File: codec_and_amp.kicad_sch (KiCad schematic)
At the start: 31 parts, among them J1 Conn_01x08, J2 Conn_01x06, U1 TLV320AIC3206IRSBR, U4 FSA2275UMX, U6 TLV7111830DSER, U7 TPD4E02B04DQAR, U8 TPD4E02B04DQAR

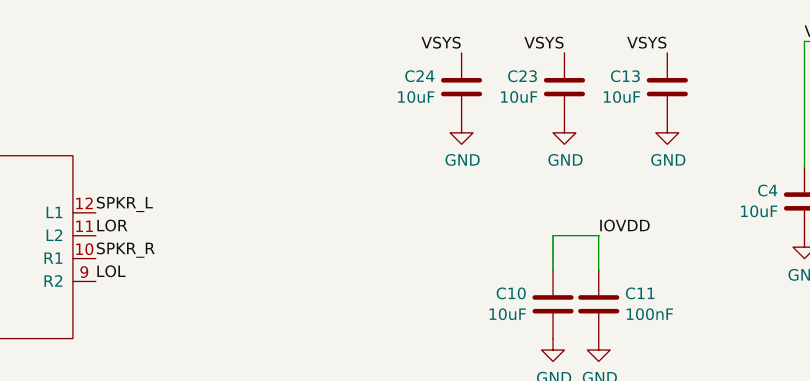
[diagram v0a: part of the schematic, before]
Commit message: Change DSI connector to the 15-pin standard instead of 22-pin standard
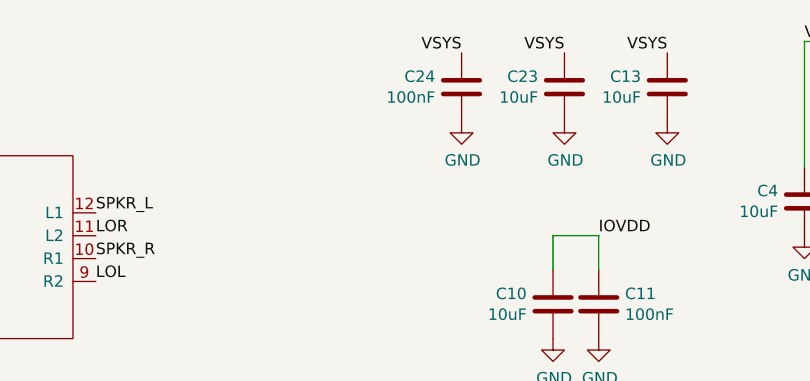
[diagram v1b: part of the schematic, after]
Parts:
- C24: value 10uF -> 100nF
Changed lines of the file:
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@@
       (effects (font (size 1.27 1.27)) (justify right))
     )
-    (property "Value" "10uF" (id 1) (at 191.389 22.733 0)
+    (property "Value" "100nF" (id 1) (at 191.389 22.733 0)
       (effects (font (size 1.27 1.27)) (justify right))
     )

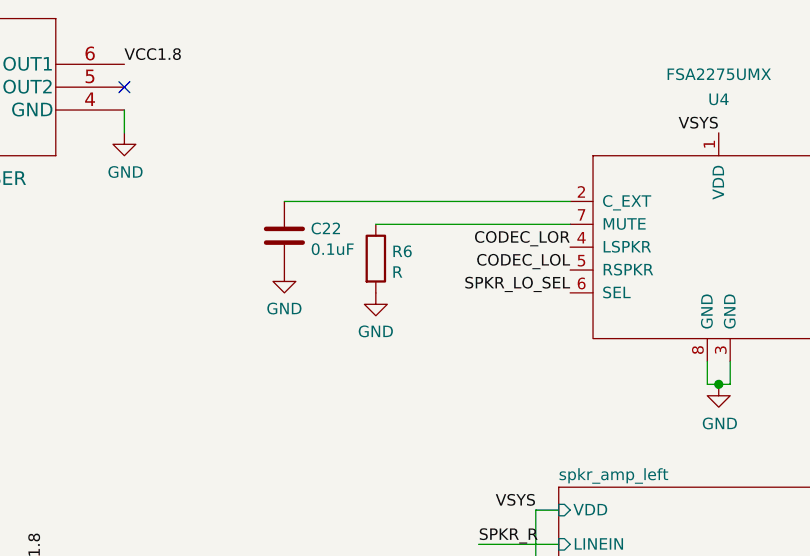
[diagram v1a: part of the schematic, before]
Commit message: Switch some footprints to minimize BOM costs. Cache a bunch more datasheets and documentation
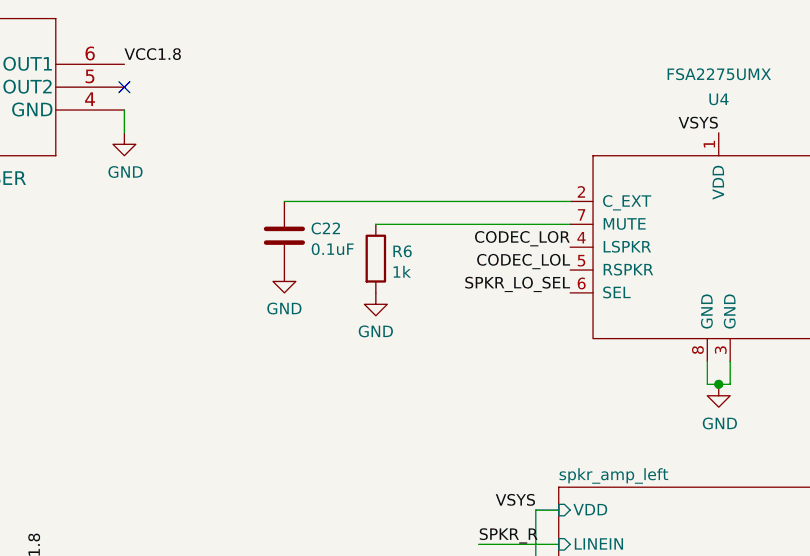
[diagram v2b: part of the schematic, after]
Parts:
- R6: value R -> 1k
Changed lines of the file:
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@@
       (effects (font (size 1.27 1.27)) (justify left))
     )
-    (property "Value" "R" (id 1) (at 100.8381 42.1778 0)
+    (property "Value" "1k" (id 1) (at 100.8381 42.1778 0)
       (effects (font (size 1.27 1.27)) (justify left))
     )

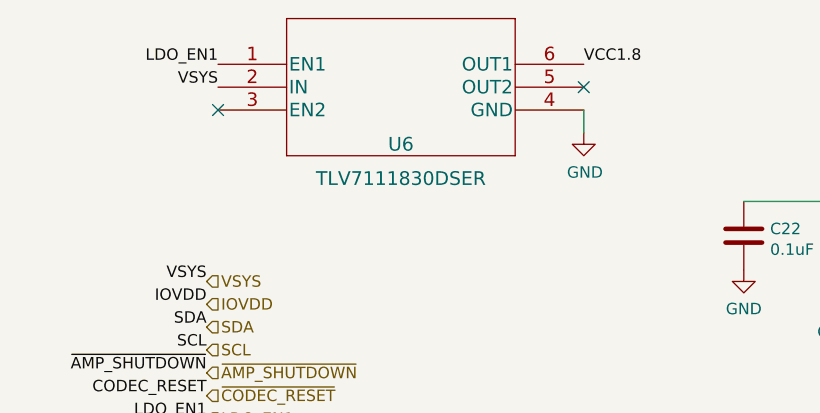
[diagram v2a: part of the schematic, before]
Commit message: Replace TLV7111830 with MIC5504, since I wasn't using that VCC3.0 and the tlv7111830 is out of stock.
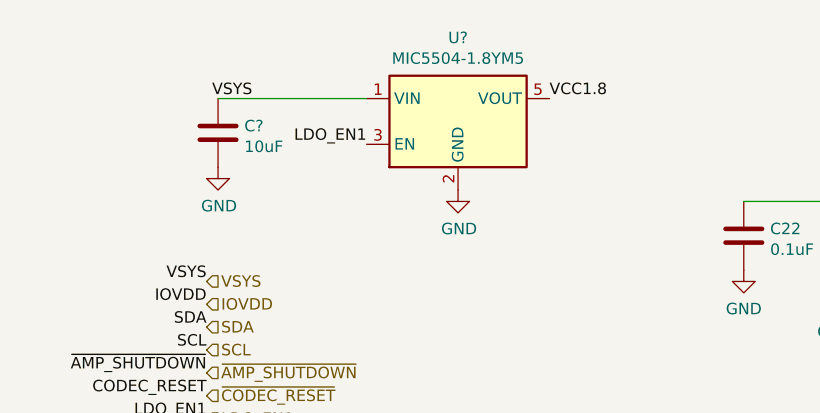
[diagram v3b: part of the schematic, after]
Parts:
- removed U6: TLV7111830DSER, footprints:TLV7111830DSER, symbol TLV7111830DSER:TLV7111830DSER
- added C?: 10uF, Capacitor_SMD:C_0402_1005Metric, symbol Device:C
- added U?: MIC5504-1.8YM5, Package_TO_SOT_SMD:SOT-23-5, symbol Regulator_Linear:MIC5504-1.8YM5
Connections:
- net GND: now also C?.2, U?.2 (GND)
- net LDO_EN1: now also U?.3 (EN)
- net VCC1.8: now also U?.5 (VOUT)
- net VSYS: now also C?.1, U?.1 (VIN)
- no-connect marks 7 -> 5
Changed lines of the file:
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@@
   (no_connect (at 29.21 104.14))
   (no_connect (at 29.21 124.46))
-  (no_connect (at 30.48 24.13))
-  (no_connect (at 71.12 21.59))
   (no_connect (at 85.09 116.84))
   (no_connect (at 85.09 139.7))
@@
     (stroke (width 0) (type solid) (color 0 0 0 0))
   )
+  (wire (pts (xy 30.48 22.86) (xy 46.99 22.86))
+    (stroke (width 0) (type solid) (color 0 0 0 0))
+  )
   (wire (pts (xy 52.07 167.64) (xy 54.61 167.64))
     (stroke (width 0) (type solid) (color 0 0 0 0))
@@
     (stroke (width 0) (type solid) (color 0 0 0 0))
   )
-  (wire (pts (xy 71.12 24.13) (xy 71.12 26.67))
-    (stroke (width 0) (type solid) (color 0 0 0 0))
-  )
   (wire (pts (xy 85.09 120.65) (xy 95.25 120.65))
     (stroke (width 0) (type solid) (color 0 0 0 0))
@@
     (effects (font (size 1.27 1.27)) (justify right bottom))
   )
-  (label "LDO_EN1" (at 30.48 19.05 180)
-    (effects (font (size 1.27 1.27)) (justify right bottom))
-  )
-  (label "VSYS" (at 30.48 21.59 180)
+  (label "VSYS" (at 34.29 22.86 180)
+    (effects (font (size 1.27 1.27)) (justify right bottom))
+  )
+  (label "LDO_EN1" (at 46.99 27.94 180)
     (effects (font (size 1.27 1.27)) (justify right bottom))
   )
@@
     (effects (font (size 1.27 1.27)) (justify left bottom))
   )
-  (label "VCC1.8" (at 71.12 19.05 0)
+  (label "VCC1.8" (at 67.31 22.86 0)
     (effects (font (size 1.27 1.27)) (justify left bottom))
   )
@@
     (pin "1")
   )
+  (symbol (lib_id "power:GND") (at 30.48 30.48 0) (unit 1)
+    (in_bom yes) (on_board yes)
+    (property "Reference" "#PWR?" (id 0) (at 30.48 36.83 0)
+      (effects (font (size 1.27 1.27)) hide)
+    )
+    (property "Value" "GND" (id 1) (at 30.5943 34.8044 0))
+    (property "Footprint" "" (id 2) (at 30.48 30.48 0)
+      (effects (font (size 1.27 1.27)) hide)
+    )
+    (property "Datasheet" "" (id 3) (at 30.48 30.48 0)
+      (effects (font (size 1.27 1.27)) hide)
+    )
+    (pin "1")
+  )
   (symbol (lib_id "power:GND") (at 38.1 175.26 0) (unit 1)
     (in_bom yes) (on_board yes)
@@
     (pin "1")
   )
+  (symbol (lib_id "power:GND") (at 57.15 33.02 0) (unit 1)
+    (in_bom yes) (on_board yes)
+    (property "Reference" "#PWR?" (id 0) (at 57.15 39.37 0)
+      (effects (font (size 1.27 1.27)) hide)
+    )
+    (property "Value" "GND" (id 1) (at 57.2643 37.3444 0))
+    (property "Footprint" "" (id 2) (at 57.15 33.02 0)
+      (effects (font (size 1.27 1.27)) hide)
+    )
+    (property "Datasheet" "" (id 3) (at 57.15 33.02 0)
+      (effects (font (size 1.27 1.27)) hide)
+    )
+    (pin "1")
+  )
   (symbol (lib_id "power:GND") (at 58.42 167.64 0) (unit 1)
     (in_bom yes) (on_board yes)
@@
     )
     (property "Datasheet" "" (id 3) (at 58.42 167.64 0)
-      (effects (font (size 1.27 1.27)) hide)
-    )
-    (pin "1")
-  )
-  (symbol (lib_id "power:GND") (at 71.12 26.67 0) (unit 1)
-    (in_bom yes) (on_board yes)
-    (property "Reference" "#PWR0111" (id 0) (at 71.12 33.02 0)
-      (effects (font (size 1.27 1.27)) hide)
-    )
-    (property "Value" "GND" (id 1) (at 71.247 31.0642 0))
-    (property "Footprint" "" (id 2) (at 71.12 26.67 0)
-      (effects (font (size 1.27 1.27)) hide)
-    )
-    (property "Datasheet" "" (id 3) (at 71.12 26.67 0)
       (effects (font (size 1.27 1.27)) hide)
     )
@@
     )
     (property "Datasheet" "~" (id 3) (at 99.06 40.64 0)
+      (effects (font (size 1.27 1.27)) hide)
+    )
+    (pin "1")
+    (pin "2")
+  )
+  (symbol (lib_id "Device:C") (at 30.48 26.67 0) (unit 1)
+    (in_bom yes) (on_board yes) (fields_autoplaced)
+    (property "Reference" "C?" (id 0) (at 33.4011 25.9091 0)
+      (effects (font (size 1.27 1.27)) (justify left))
+    )
+    (property "Value" "10uF" (id 1) (at 33.4011 28.2078 0)
+      (effects (font (size 1.27 1.27)) (justify left))
+    )
+    (property "Footprint" "Capacitor_SMD:C_0402_1005Metric" (id 2) (at 31.4452 30.48 0)
+      (effects (font (size 1.27 1.27)) hide)
+    )
+    (property "Datasheet" "~" (id 3) (at 30.48 26.67 0)
       (effects (font (size 1.27 1.27)) hide)
     )
@@
     (pin "8")
   )
-  (symbol (lib_id "TLV7111830DSER:TLV7111830DSER") (at 30.48 19.05 0) (unit 1)
-    (in_bom yes) (on_board yes)
-    (property "Reference" "U6" (id 0) (at 50.8 27.94 0)
-      (effects (font (size 1.524 1.524)))
-    )
-    (property "Value" "TLV7111830DSER" (id 1) (at 50.8 31.75 0)
-      (effects (font (size 1.524 1.524)))
-    )
-    (property "Footprint" "footprints:TLV7111830DSER" (id 2) (at 50.8 12.954 0)
-      (effects (font (size 1.524 1.524)) hide)
-    )
-    (property "Datasheet" "" (id 3) (at 30.48 19.05 0)
-      (effects (font (size 1.524 1.524)))
+  (symbol (lib_id "Regulator_Linear:MIC5504-1.8YM5") (at 57.15 25.4 0) (unit 1)
+    (in_bom yes) (on_board yes)
+    (property "Reference" "U?" (id 0) (at 57.15 16.1098 0))
+    (property "Value" "MIC5504-1.8YM5" (id 1) (at 57.15 18.4085 0))
+    (property "Footprint" "Package_TO_SOT_SMD:SOT-23-5" (id 2) (at 57.15 35.56 0)
+      (effects (font (size 1.27 1.27)) hide)
+    )
+    (property "Datasheet" "http://ww1.microchip.com/downloads/en/DeviceDoc/MIC550X.pdf" (id 3) (at 50.8 19.05 0)
+      (effects (font (size 1.27 1.27)) hide)
     )
     (pin "1")
@@
     (pin "4")
     (pin "5")
-    (pin "6")
   )
   (symbol (lib_id "TPD4E02B04DQAR:TPD4E02B04DQAR") (at 233.68 106.68 0) (unit 1)

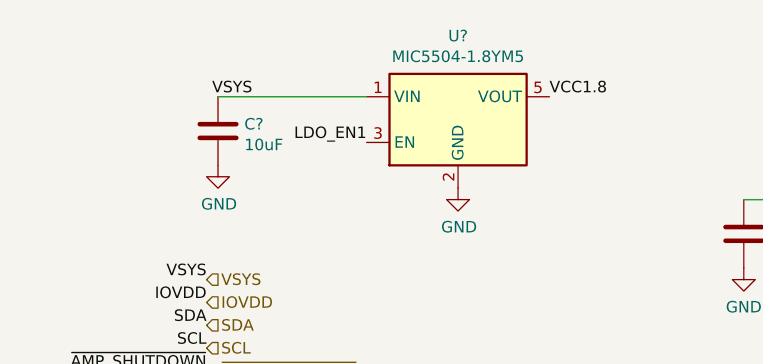
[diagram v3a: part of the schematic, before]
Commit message: add usb otg connector for testing usb wiring; fix more ERC/DRC
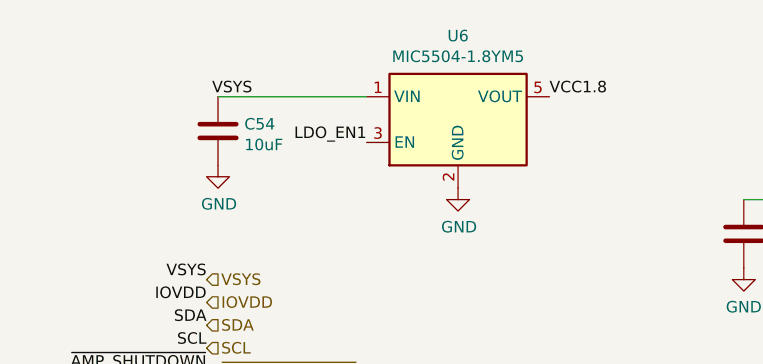
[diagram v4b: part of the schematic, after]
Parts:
- gave numbers to parts that had none: 2
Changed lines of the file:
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@@
   (symbol (lib_id "power:GND") (at 30.48 30.48 0) (unit 1)
     (in_bom yes) (on_board yes)
-    (property "Reference" "#PWR?" (id 0) (at 30.48 36.83 0)
+    (property "Reference" "#PWR039" (id 0) (at 30.48 36.83 0)
       (effects (font (size 1.27 1.27)) hide)
     )
@@
   (symbol (lib_id "power:GND") (at 57.15 33.02 0) (unit 1)
     (in_bom yes) (on_board yes)
-    (property "Reference" "#PWR?" (id 0) (at 57.15 39.37 0)
+    (property "Reference" "#PWR040" (id 0) (at 57.15 39.37 0)
       (effects (font (size 1.27 1.27)) hide)
     )
@@
   (symbol (lib_id "Device:C") (at 30.48 26.67 0) (unit 1)
     (in_bom yes) (on_board yes) (fields_autoplaced)
-    (property "Reference" "C?" (id 0) (at 33.4011 25.9091 0)
+    (property "Reference" "C54" (id 0) (at 33.4011 25.9091 0)
       (effects (font (size 1.27 1.27)) (justify left))
     )
@@
   (symbol (lib_id "Regulator_Linear:MIC5504-1.8YM5") (at 57.15 25.4 0) (unit 1)
     (in_bom yes) (on_board yes)
-    (property "Reference" "U?" (id 0) (at 57.15 16.1098 0))
+    (property "Reference" "U6" (id 0) (at 57.15 16.1098 0))
     (property "Value" "MIC5504-1.8YM5" (id 1) (at 57.15 18.4085 0))
     (property "Footprint" "Package_TO_SOT_SMD:SOT-23-5" (id 2) (at 57.15 35.56 0)

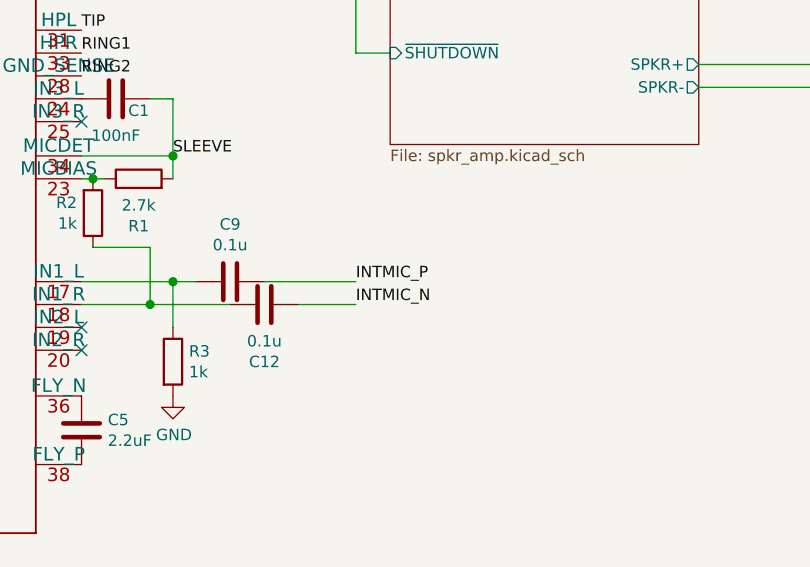
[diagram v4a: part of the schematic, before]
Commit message: WIP: start reworking board to use CM4 instead of 40-pin connector
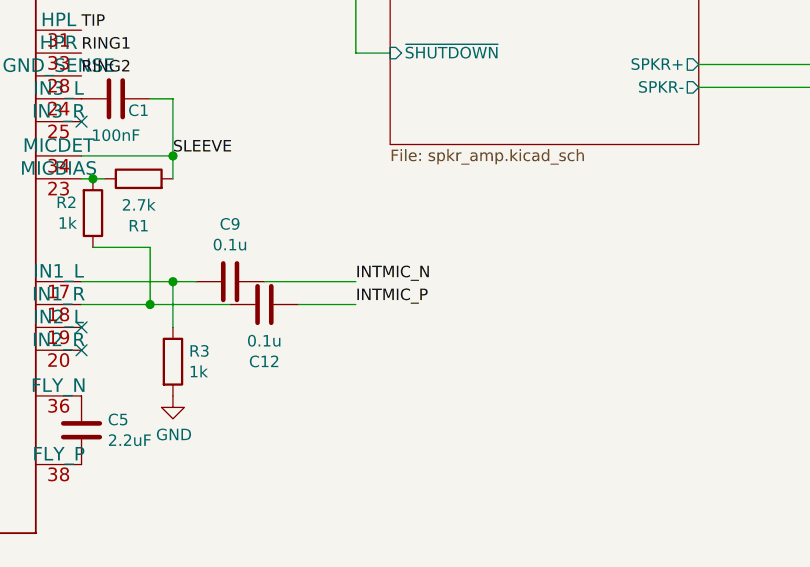
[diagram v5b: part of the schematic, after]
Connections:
- net INTMIC_N: now also C9.2; no longer C12.2
- net INTMIC_P: now also C12.2; no longer C9.2
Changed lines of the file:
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@@
     (effects (font (size 1.27 1.27)) (justify left bottom))
   )
-  (label "INTMIC_P" (at 115.57 134.62 0)
+  (label "INTMIC_N" (at 115.57 134.62 0)
     (effects (font (size 1.27 1.27)) (justify left bottom))
   )
-  (label "INTMIC_N" (at 115.57 137.16 0)
+  (label "INTMIC_P" (at 115.57 137.16 0)
     (effects (font (size 1.27 1.27)) (justify left bottom))
   )

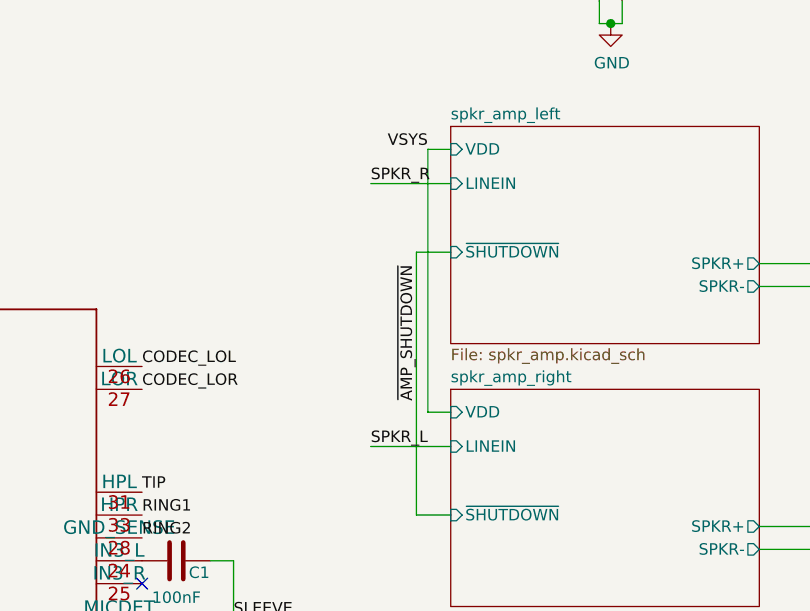
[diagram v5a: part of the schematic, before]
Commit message: Lots of changes: add USB switch in charger circuit, reroute differential pairs using proper track widths; make CM4 courtyard the full size. Fixes #11.
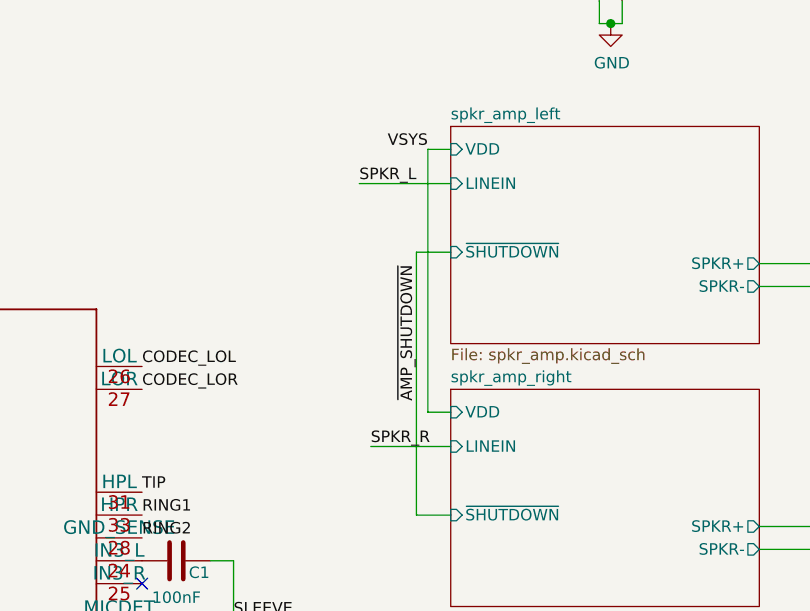
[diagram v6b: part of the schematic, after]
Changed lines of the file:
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@@
+    (stroke (width 0) (type solid) (color 0 0 0 0))
+  )
+  (wire (pts (xy 109.22 72.39) (xy 119.38 72.39))
     (stroke (width 0) (type solid) (color 0 0 0 0))
   )
@@
     (stroke (width 0) (type solid) (color 0 0 0 0))
   )
-  (wire (pts (xy 110.49 72.39) (xy 119.38 72.39))
-    (stroke (width 0) (type solid) (color 0 0 0 0))
-  )
   (wire (pts (xy 110.49 101.6) (xy 119.38 101.6))
     (stroke (width 0) (type solid) (color 0 0 0 0))
@@
     (effects (font (size 1.27 1.27)) (justify left bottom))
   )
-  (label "SPKR_R" (at 110.49 72.39 0)
-    (effects (font (size 1.27 1.27)) (justify left bottom))
-  )
-  (label "SPKR_L" (at 110.49 101.6 0)
-    (effects (font (size 1.27 1.27)) (justify left bottom))
-  )
+  (label "SPKR_L" (at 109.22 72.39 0)
+    (effects (font (size 1.27 1.27)) (justify left bottom))
+  )
+  (label "SPKR_R" (at 110.49 101.6 0)
+    (effects (font (size 1.27 1.27)) (justify left bottom))
+  )
